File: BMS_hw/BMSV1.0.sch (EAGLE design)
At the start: 161 parts, among them IC1 MC33771BEP, IC2 SFH6156, J2 NTC, X2 87758-1816

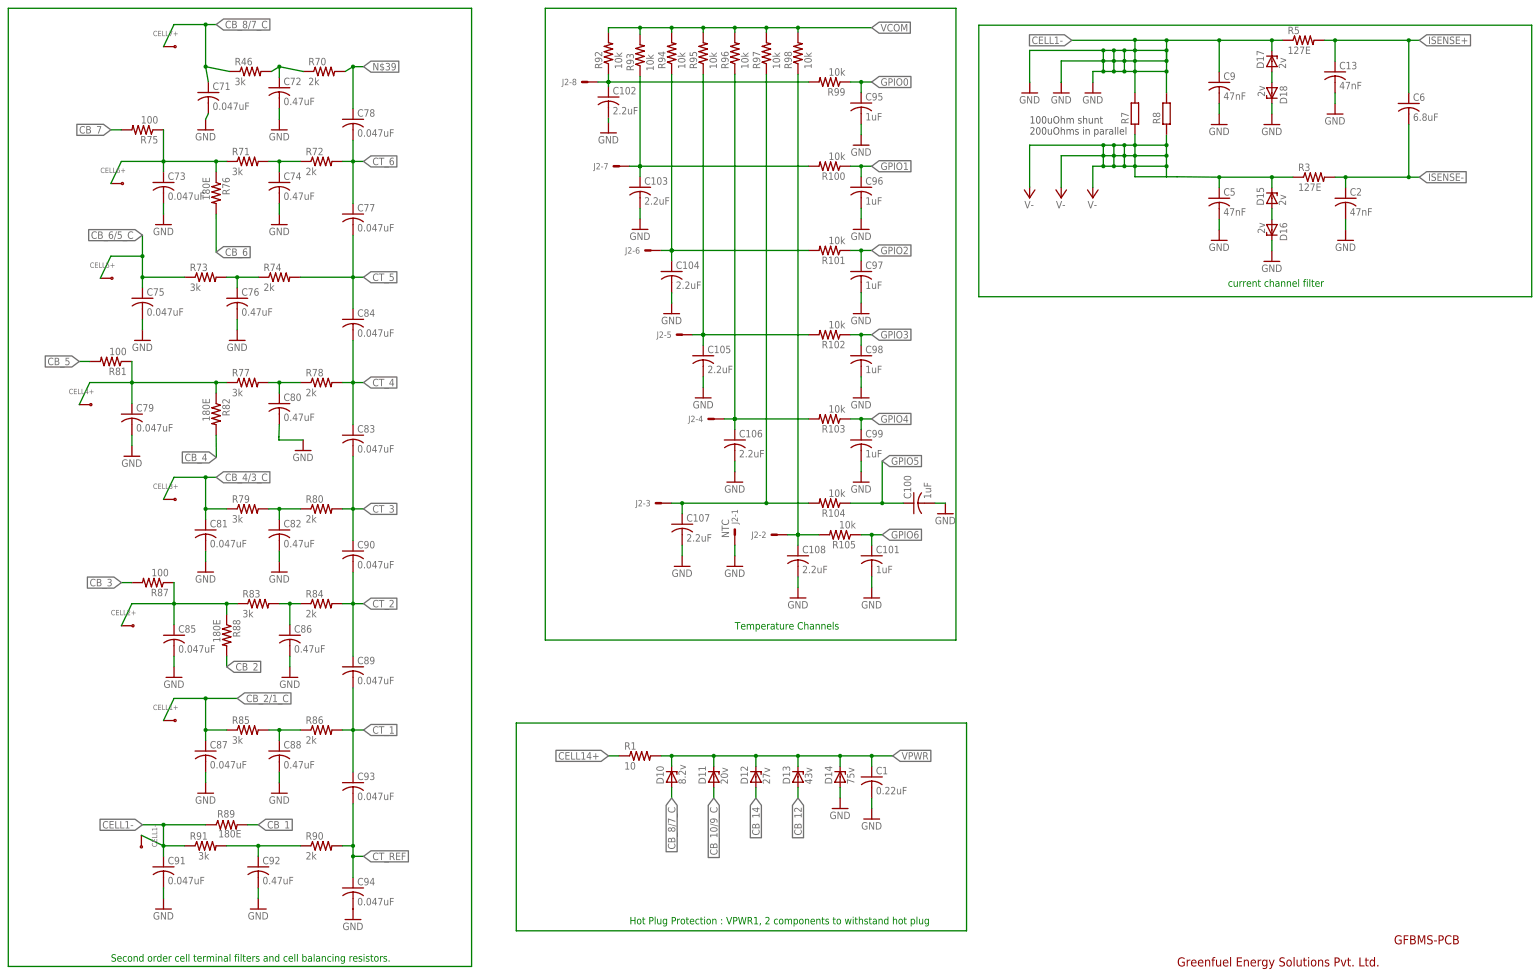
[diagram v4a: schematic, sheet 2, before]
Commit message: hot plug protection and other protection schematic offgrid corrected
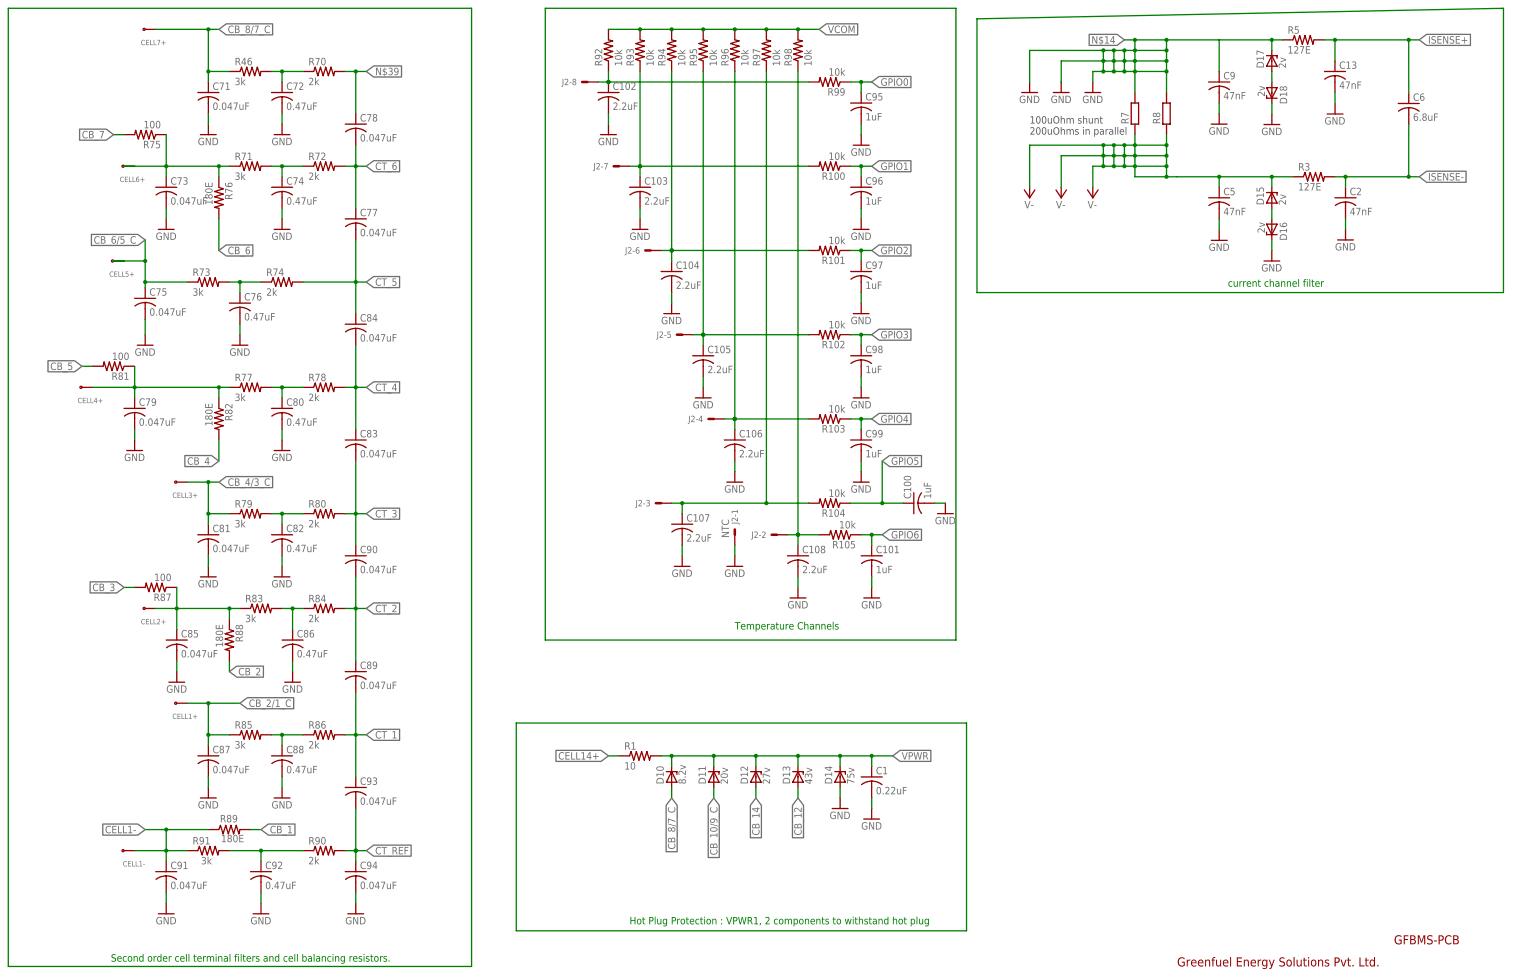
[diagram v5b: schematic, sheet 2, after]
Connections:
- removed net N$10: C5.1, D15.C, R3.1
- new net N$14: C9.1, R7.2, R8.2
- new net N$15: D17.C, R5.1
- net CELL1-: no longer C9.1, D17.C, R5.1
- net GND: no longer R7.2
- net V-: now also C5.1, D15.C, R3.1, R8.1
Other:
- moved on the sheet: C102, C72, C73, C74, C75, C76, C77, C78, C79, C80, C81, C82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

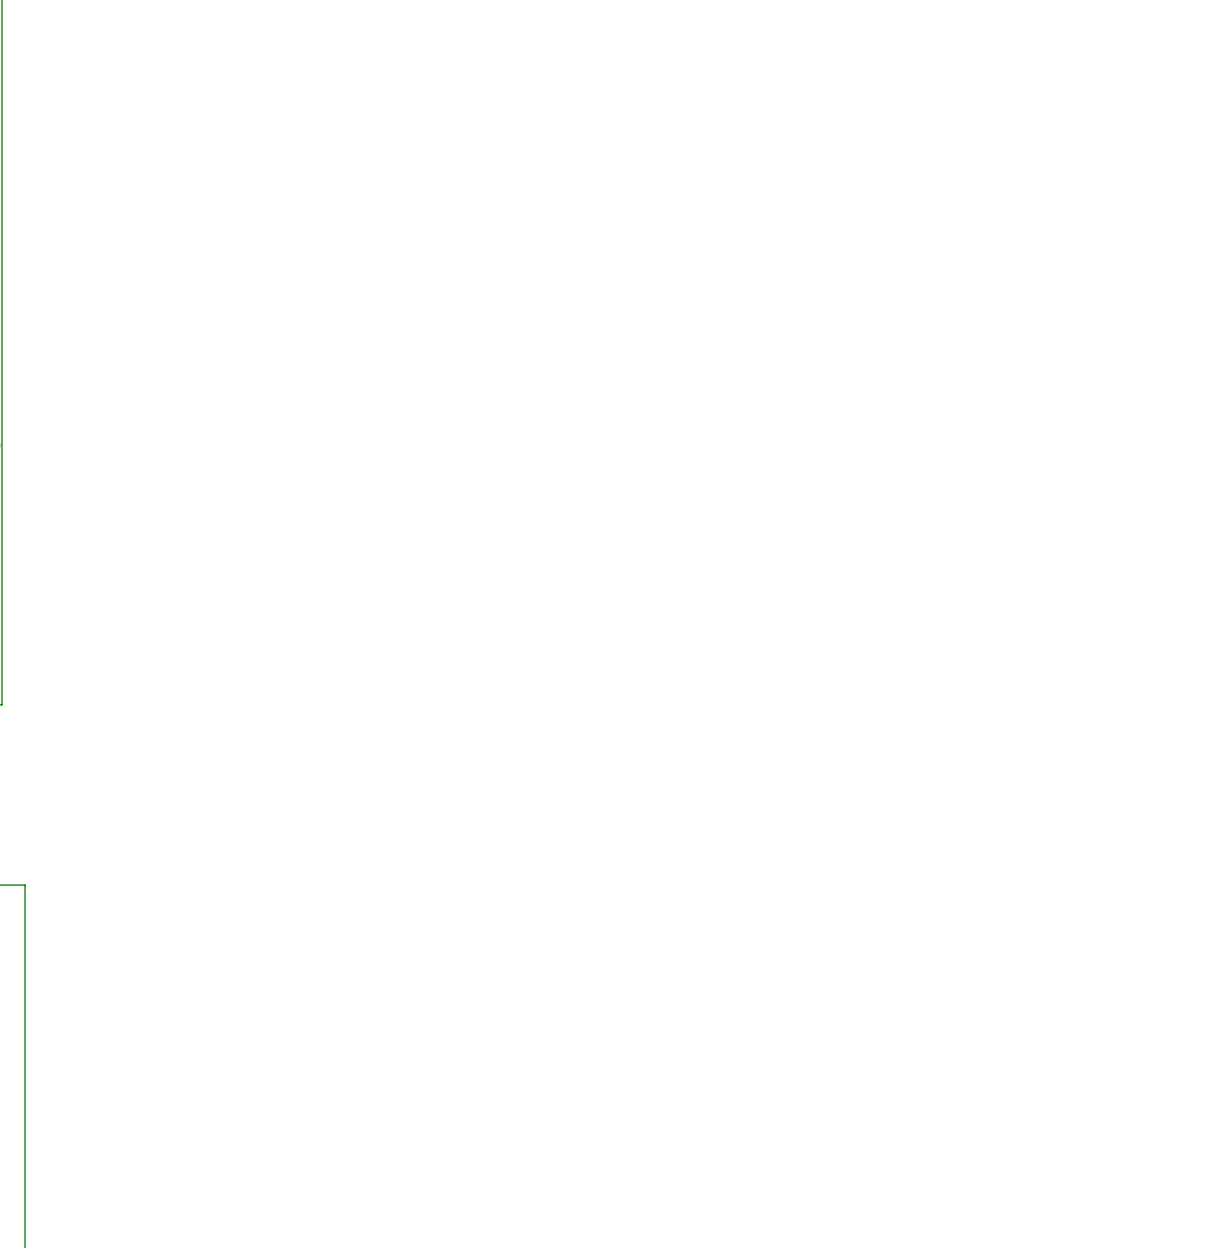
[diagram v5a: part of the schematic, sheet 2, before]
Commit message: Buck convertor schematic added on page 2
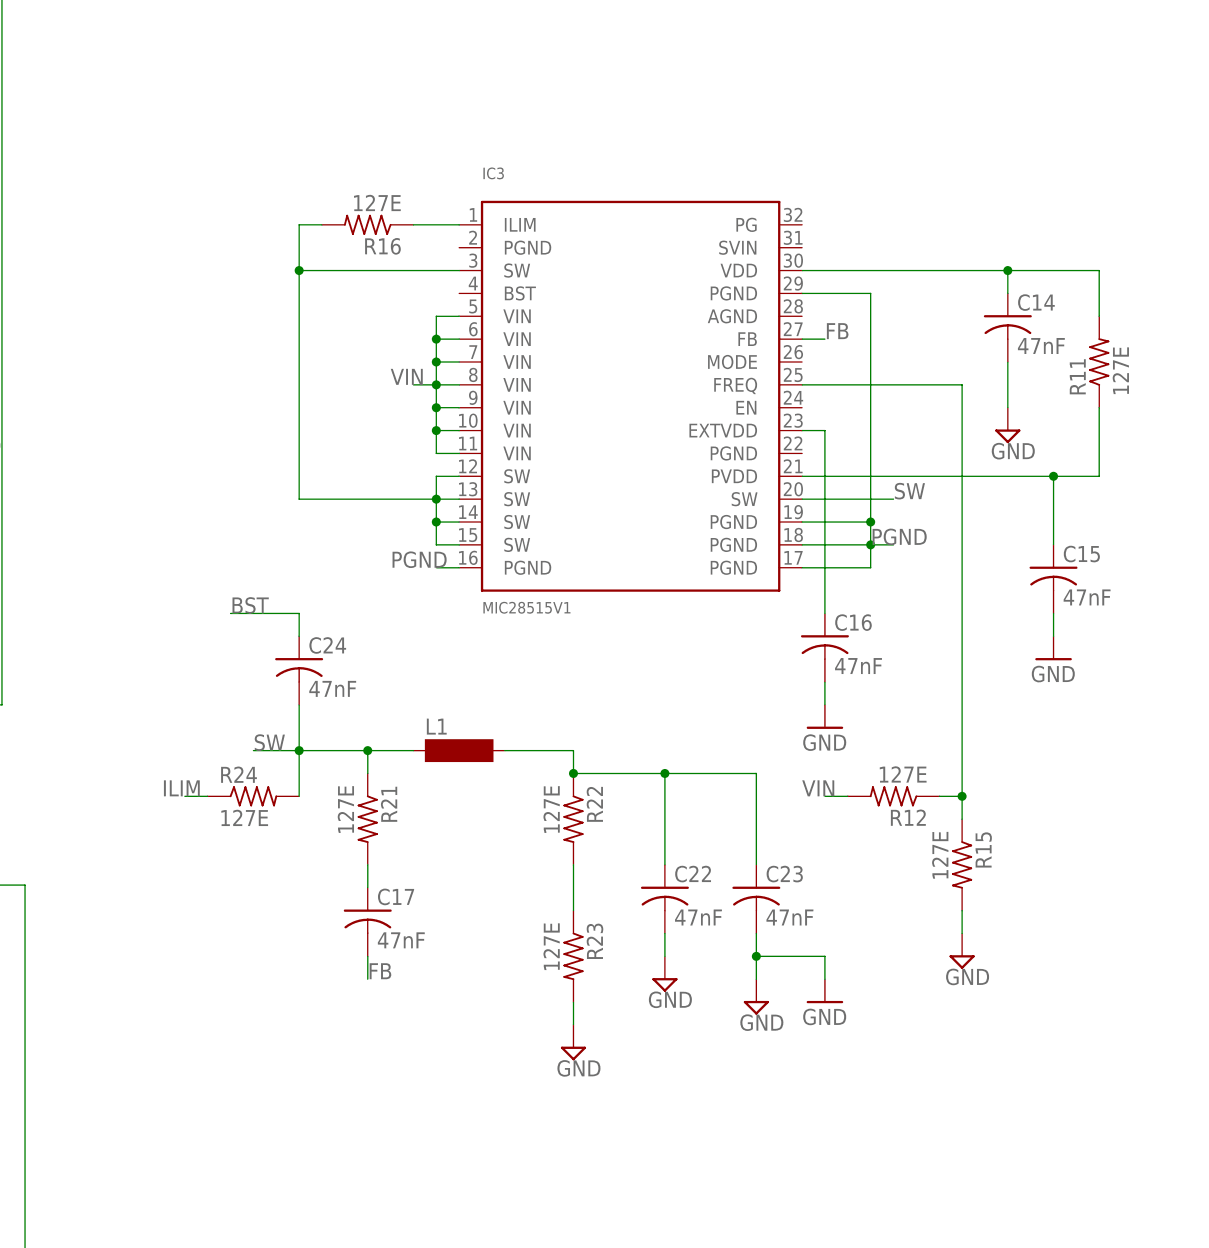
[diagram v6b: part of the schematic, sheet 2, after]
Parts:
- added C14, C15, C16, C17, C22, C23, C24: 47nF, adafruit:C-USC0805
- added IC3: MIC28515V1, GreenFuel:MIC28515V1
- added L1: (no value), inductor-neosid:MS85
- added R11, R12, R15, R16, R21, R22, R23, R24: 127E, adafruit:R-US_R0805
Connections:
- new net BST: C24.1
- new net FB: C17.2, IC3.FB
- new net ILIM: R24.1
- new net N$10: C14.1, IC3.VDD, R11.2
- new net N$16: C15.1, IC3.PVDD, R11.1
- new net N$17: IC3.FREQ, R12.1, R15.1
- new net N$18: C16.1, IC3.EXTVDD
- new net N$19: IC3.ILIM, R16.1
- new net N$20: IC3.SW, IC3.SW@1, IC3.SW@2, IC3.SW@3, IC3.SW@4, R16.2
- new net N$21: C22.1, C23.1, L1.2, R22.1
- new net N$22: R22.2, R23.1
- new net N$24: C17.1, R21.2
- new net PGND: IC3.PGND@1, IC3.PGND@2, IC3.PGND@3, IC3.PGND@4, IC3.PGND@6
- new net SW: C24.2, IC3.SW@5, L1.1, R21.1, R24.2
- new net VIN: IC3.VIN, IC3.VIN@1, IC3.VIN@2, IC3.VIN@3, IC3.VIN@4, IC3.VIN@5, IC3.VIN@6, R12.2
- net GND: now also C14.2, C15.2, C16.2, C22.2, C23.2, R15.2, R23.2

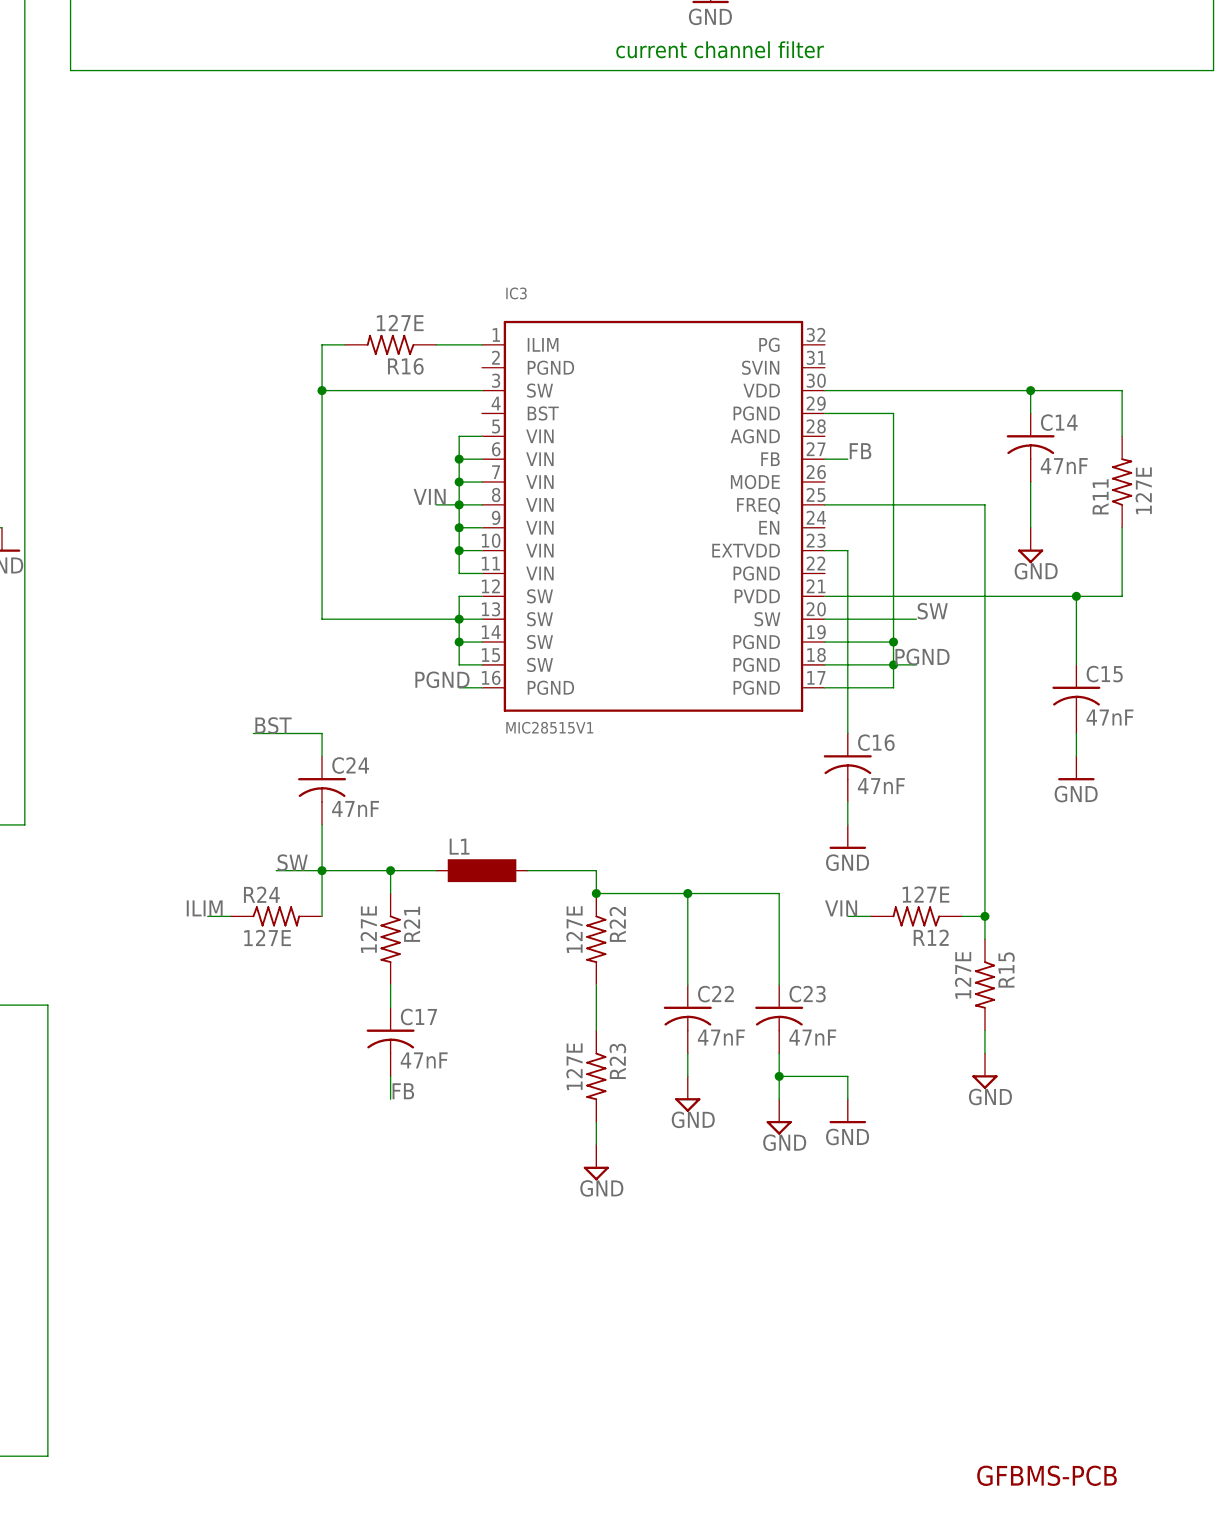
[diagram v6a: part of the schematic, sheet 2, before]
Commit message: Buck convertor schematic complete calaculation required!
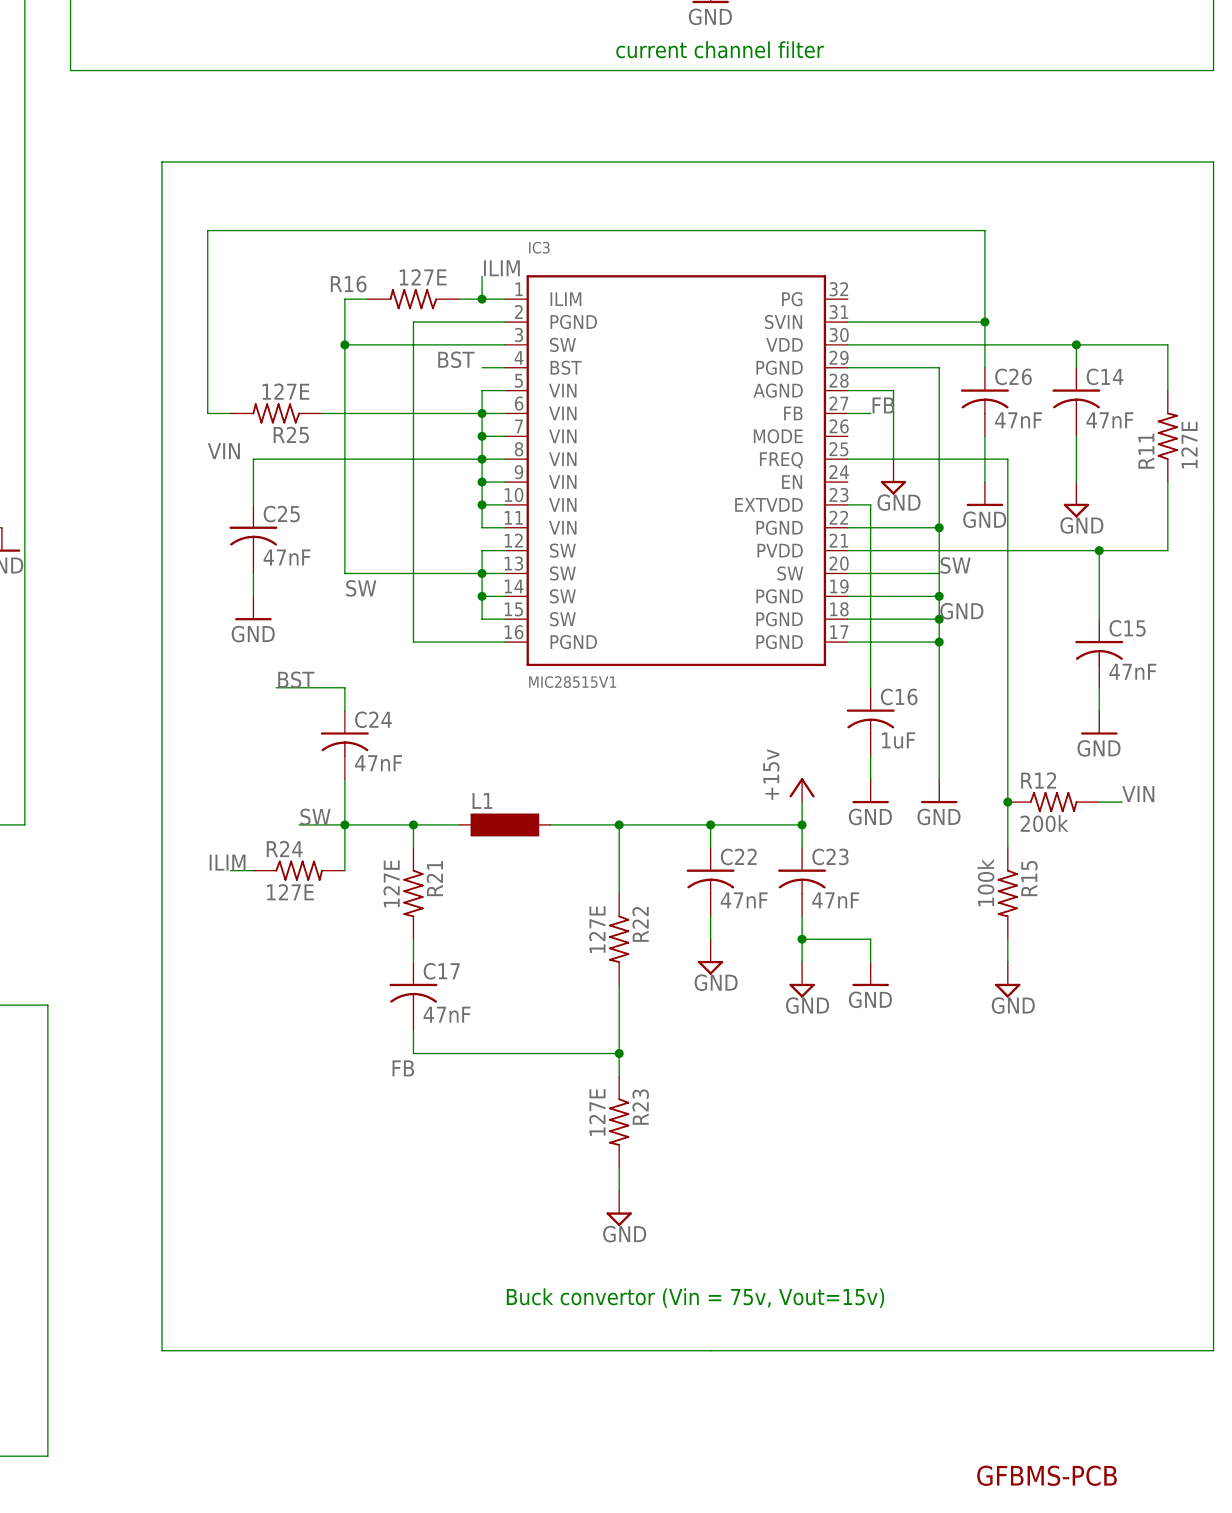
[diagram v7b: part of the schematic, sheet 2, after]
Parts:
- added C25, C26: 47nF, adafruit:C-USC0805
- added R25: 127E, adafruit:R-US_R0805
- C16: value 47nF -> 1uF
- R12: value 127E -> 200k
- R15: value 127E -> 100k
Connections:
- net N$21 renamed VCC
- removed net N$19: IC3.ILIM, R16.1
- removed net N$22: R22.2, R23.1
- removed net PGND: IC3.PGND@1, IC3.PGND@2, IC3.PGND@3, IC3.PGND@4, IC3.PGND@6
- new net N$21: C26.1, IC3.SVIN, R25.2
- net BST: now also IC3.BST
- net FB: now also R22.2, R23.1
- net GND: now also C25.2, C26.2, IC3.AGND, IC3.PGND@2, IC3.PGND@3, IC3.PGND@4, IC3.PGND@5, IC3.PGND@6
- net ILIM: now also IC3.ILIM, R16.1
- net N$20: now also IC3.PGND, IC3.PGND@1; no longer IC3.SW, IC3.SW@1, IC3.SW@2, IC3.SW@3, IC3.SW@4, R16.2
- net SW: now also IC3.SW, IC3.SW@1, IC3.SW@2, IC3.SW@3, IC3.SW@4, R16.2
- net VIN: now also C25.1, R25.1
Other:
- note added: "Buck convertor (Vin = 75v, Vout=15v)"
- moved on the sheet: C14, C15, C16, C17, C22, C23, C24, IC3, L1, R11, R12, R15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
